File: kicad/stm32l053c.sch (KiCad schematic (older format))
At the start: 37 parts, among them J1 GND, J10 3V3, J11 I2C, J2 GND, J3 TX, J4 GND, J5 TEST_1P, J6 TEST_1P, J8 RX, P1 SWD, U2 STM32L053C8_LQFP48, U3 ADS1015, U4 UFL_SMA, U5 RFM92/95

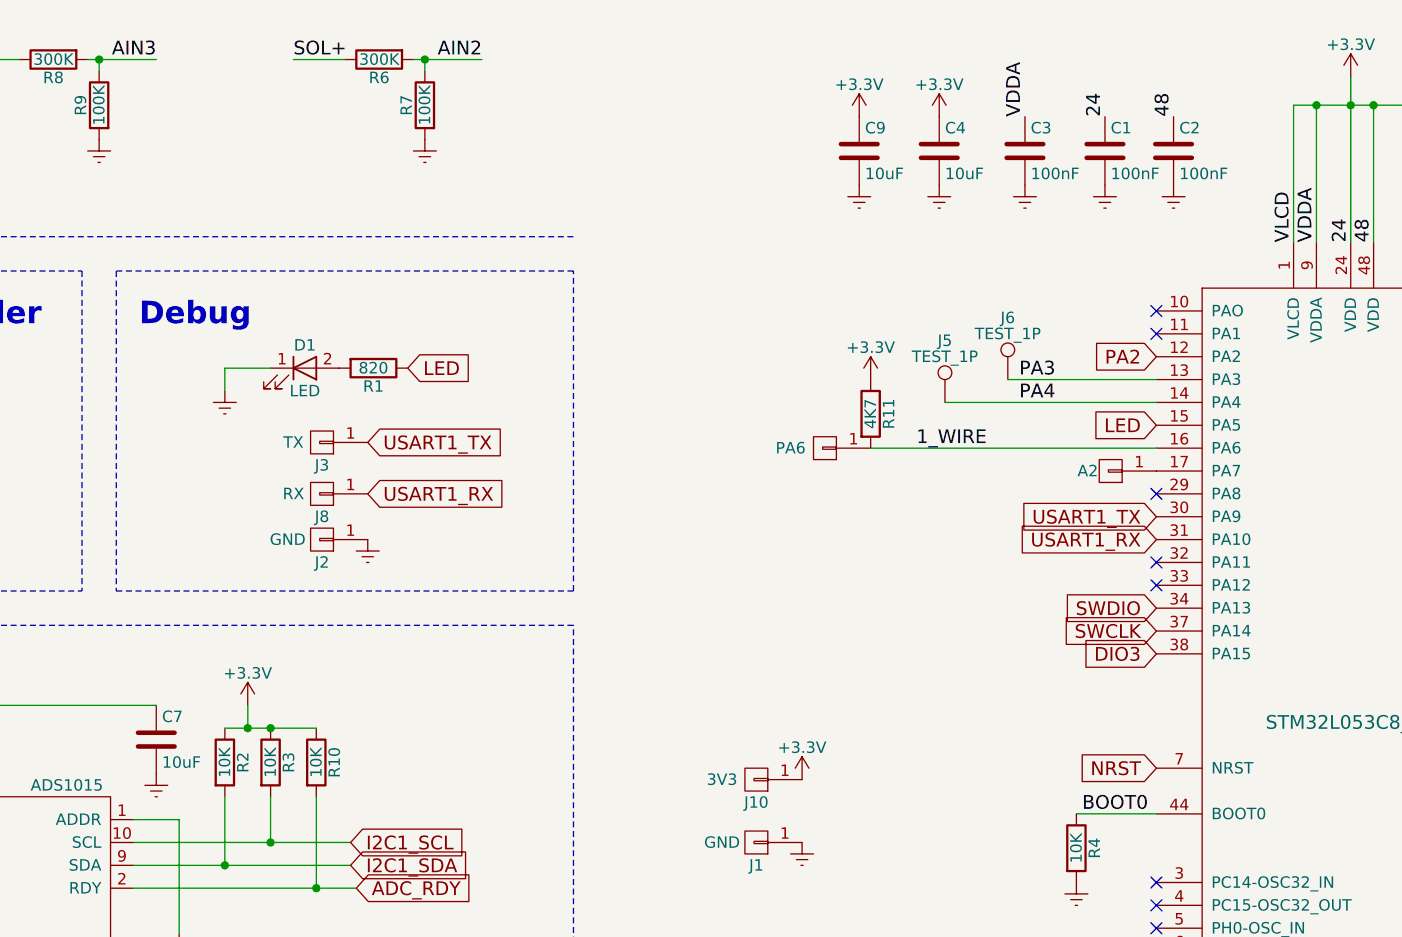
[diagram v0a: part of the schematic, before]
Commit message: 0.1uF bypass cap
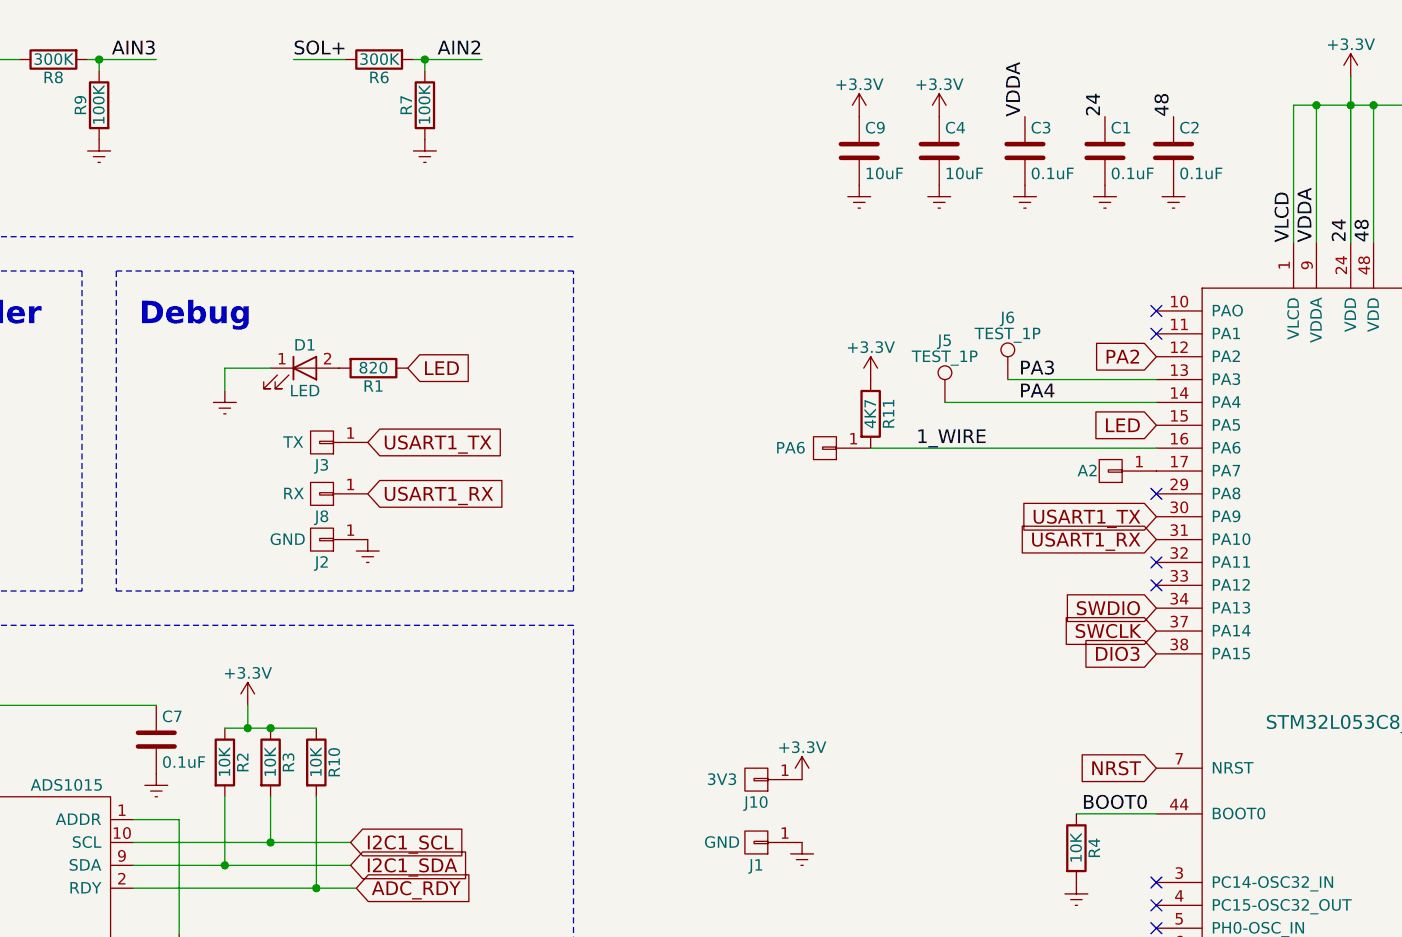
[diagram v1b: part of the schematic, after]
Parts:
- C1, C2, C3: value 100nF -> 0.1uF
- C7: value 10uF -> 0.1uF
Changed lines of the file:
@@
 P 7400 1750
 F 0 "C1" H 7425 1850 50  0000 L CNN
-F 1 "100nF" H 7425 1650 50  0000 L CNN
+F 1 "0.1uF" H 7425 1650 50  0000 L CNN
 F 2 "Capacitors_SMD:C_0805_HandSoldering" H 7438 1600 50  0001 C CNN
 F 3 "" H 7400 1750 50  0000 C CNN
@@
 P 7700 1750
 F 0 "C2" H 7725 1850 50  0000 L CNN
-F 1 "100nF" H 7725 1650 50  0000 L CNN
+F 1 "0.1uF" H 7725 1650 50  0000 L CNN
 F 2 "Capacitors_SMD:C_0805_HandSoldering" H 7738 1600 50  0001 C CNN
 F 3 "" H 7700 1750 50  0000 C CNN
@@
 P 7050 1750
 F 0 "C3" H 7075 1850 50  0000 L CNN
-F 1 "100nF" H 7075 1650 50  0000 L CNN
+F 1 "0.1uF" H 7075 1650 50  0000 L CNN
 F 2 "Capacitors_SMD:C_0805_HandSoldering" H 7088 1600 50  0001 C CNN
 F 3 "" H 7050 1750 50  0000 C CNN
@@
 P 3250 4325
 F 0 "C7" H 3275 4425 50  0000 L CNN
-F 1 "10uF" H 3275 4225 50  0000 L CNN
+F 1 "0.1uF" H 3275 4225 50  0000 L CNN
 F 2 "Capacitors_SMD:C_0805_HandSoldering" H 3288 4175 50  0001 C CNN
 F 3 "" H 3250 4325 50  0001 C CNN

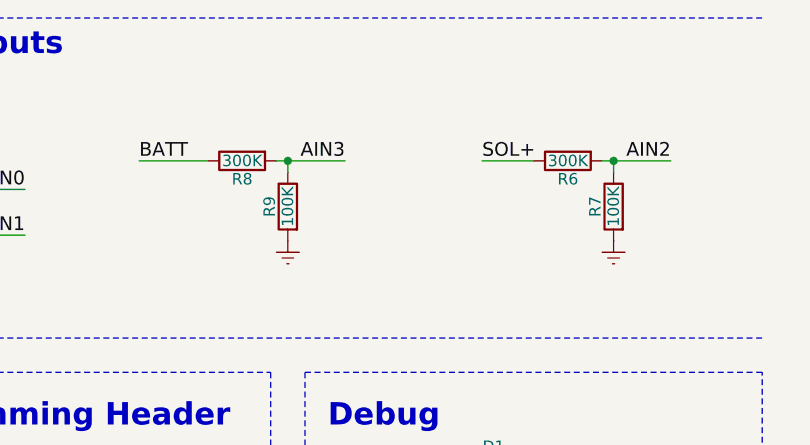
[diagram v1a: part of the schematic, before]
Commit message: External ADC with 620/100 voltage divider
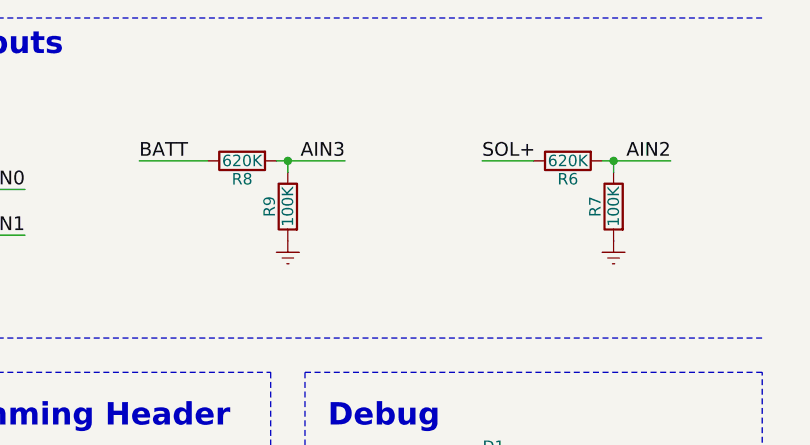
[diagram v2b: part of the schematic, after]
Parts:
- R6, R8: value 300K -> 620K
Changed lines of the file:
@@
 P 4225 1350
 F 0 "R6" V 4305 1350 50  0000 C CNN
-F 1 "300K" V 4225 1350 50  0000 C CNN
+F 1 "620K" V 4225 1350 50  0000 C CNN
 F 2 "Resistors_SMD:R_0805_HandSoldering" V 4155 1350 50  0001 C CNN
 F 3 "" H 4225 1350 50  0001 C CNN
@@
 P 2800 1350
 F 0 "R8" V 2880 1350 50  0000 C CNN
-F 1 "300K" V 2800 1350 50  0000 C CNN
+F 1 "620K" V 2800 1350 50  0000 C CNN
 F 2 "Resistors_SMD:R_0805_HandSoldering" V 2730 1350 50  0001 C CNN
 F 3 "" H 2800 1350 50  0001 C CNN

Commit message: AIN headers
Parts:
- removed R5: R_Shunt, theapi:SHUNT_1210_HandSoldering, symbol R_Shunt
- added J12: AIN, Pin_Headers:Pin_Header_Straight_1x01_Pitch2.54mm, symbol Conn_01x01
- added J13: SOL_SENSE_L, Pin_Headers:Pin_Header_Straight_1x01_Pitch2.54mm, symbol Conn_01x01
- added J7: BATT_SENSE, Pin_Headers:Pin_Header_Straight_1x01_Pitch2.54mm, symbol Conn_01x01
- added J9: SOL_SENSE_H, Pin_Headers:Pin_Header_Straight_1x01_Pitch2.54mm, symbol Conn_01x01
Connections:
- net AIN0: now also J9.1 (Pin_1)
- net AIN1: now also J13.1 (Pin_1)
- net BATT: now also J7.1 (Pin_1)
- net PA2 renamed USART2_TX
- net PA3 renamed USART2_RX
- net SOL+ renamed AIN
- net AIN: now also J12.1 (Pin_1)
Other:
- note added: "External shunt on\nLOW SIDE\nof the solar panel"
- moved on the sheet: D1, J2, J3, J6, J8, P1, R1, R6, R7, R8, R9
